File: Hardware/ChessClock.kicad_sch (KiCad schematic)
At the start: 0 parts

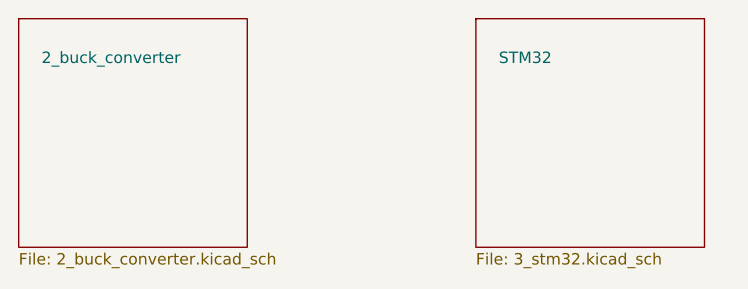
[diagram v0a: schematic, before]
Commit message: Change kicad folder name to hardware
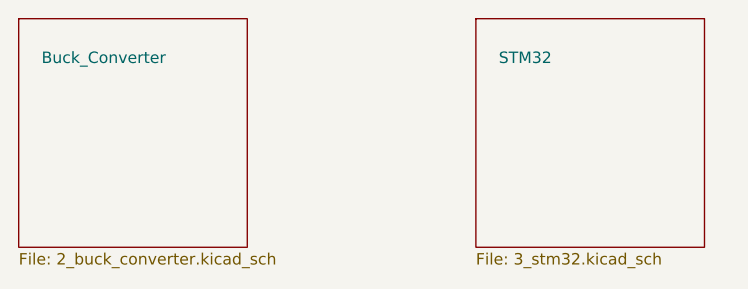
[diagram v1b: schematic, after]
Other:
- sheet 2_buck_converter renamed Buck_Converter
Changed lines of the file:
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@@
     (stroke (width 0.1524) (type solid) (color 0 0 0 0))
     (fill (color 255 229 191 1.0000))
-    (property "Sheet name" "2_buck_converter" (id 0) (at 53.34 55.88 0)
+    (property "Sheet name" "Buck_Converter" (id 0) (at 53.34 55.88 0)
       (effects (font (size 1.27 1.27)) (justify left bottom))
     )
